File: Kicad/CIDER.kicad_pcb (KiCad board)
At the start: 2 copper layers, 0 parts

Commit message: PCB: Start routing PCB
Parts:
- added C1: 0.1u, Capacitor_SMD:C_0603_1608Metric, F.Cu at (84.9, 113.6)
- added C10: 0.1u, Capacitor_SMD:C_0603_1608Metric, F.Cu at (53.5, 110.0)
- added C11: 0.1u, Capacitor_SMD:C_0603_1608Metric, F.Cu at (76.8, 146.8)
- added C12: 0.1u, Capacitor_SMD:C_0603_1608Metric, F.Cu at (230.0, 102.8)
- added C13: 0.1u, Capacitor_SMD:C_0603_1608Metric, F.Cu at (222.0, 105.3)
- added C14: 0.1u, Capacitor_SMD:C_0603_1608Metric, F.Cu at (218.0, 102.8)
- added C15: 10u, Capacitor_SMD:C_0805_2012Metric_Pad1.18x1.45mm_HandSolder, F.Cu at (222.7, 152.0)
- added C16: 10u, Capacitor_SMD:C_0805_2012Metric_Pad1.18x1.45mm_HandSolder, F.Cu at (199.3, 183.9)
- added C17: 0.1u, Capacitor_SMD:C_0603_1608Metric, F.Cu at (207.7, 175.6)
- added C18: 0.1u, Capacitor_SMD:C_0603_1608Metric, F.Cu at (213.5, 164.9)
- added C19: 0.1u, Capacitor_SMD:C_0603_1608Metric, F.Cu at (222.3, 154.8)
- added C2: 10u, Capacitor_SMD:C_0805_2012Metric_Pad1.18x1.45mm_HandSolder, F.Cu at (86.4, 108.2)
- added C20: 0.1u, Capacitor_SMD:C_0603_1608Metric, F.Cu at (227.1, 151.8)
- added C21: 0.1u, Capacitor_SMD:C_0603_1608Metric, F.Cu at (217.5, 159.8)
- added C22: 0.1u, Capacitor_SMD:C_0603_1608Metric, F.Cu at (198.9, 186.6)
- added C23: 0.1u, Capacitor_SMD:C_0603_1608Metric, F.Cu at (213.5, 162.4)
- added C24: 0.1u, Capacitor_SMD:C_0603_1608Metric, F.Cu at (213.5, 159.8)
- added C25: 0.1u, Capacitor_SMD:C_0603_1608Metric, F.Cu at (226.3, 154.8)
- added C26: 0.1u, Capacitor_SMD:C_0603_1608Metric, F.Cu at (147.0, 165.3)
- added C27: 0.1u, Capacitor_SMD:C_0603_1608Metric, F.Cu at (131.0, 174.9)
- added C3: 0.1u, Capacitor_SMD:C_0603_1608Metric, F.Cu at (91.7, 133.6)
- added C4: 0.1u, Capacitor_SMD:C_0603_1608Metric, F.Cu at (53.5, 107.5)
- added C5: 10u, Capacitor_Tantalum_SMD:CP_EIA-3216-18_Kemet-A, F.Cu at (202.4, 95.1)
- added C6: 0.1u, Capacitor_SMD:C_0603_1608Metric, F.Cu at (87.7, 136.1)
- added C7: 0.1u, Capacitor_SMD:C_0603_1608Metric, F.Cu at (87.7, 133.6)
- added C8: 0.1u, Capacitor_SMD:C_0603_1608Metric, F.Cu at (84.9, 111.1)
- added C9: 10u, Capacitor_Tantalum_SMD:CP_EIA-3216-18_Kemet-A, F.Cu at (81.1, 108.3)
- added CN1: CDTV-DIAG, KEL-8800-080-170SF:KEL-8800-080-170S, B.Cu at (147.3, 99.1)
- added F1: Polyfuse 500mA Hold, Fuse:Fuse_1206_3216Metric, F.Cu at (245.0, 95.1)
- added J1: Conn_01x06_Male, Connector_PinHeader_2.54mm:PinHeader_1x06_P2.54mm_Vertical, F.Cu at (177.9, 106.5)
- added J2: LED, Connector_PinHeader_2.54mm:PinHeader_1x02_P2.54mm_Vertical, F.Cu at (212.2, 141.9)
- added J3: Conn_02x22_Odd_Even, Connector_PinHeader_2.00mm:PinHeader_2x22_P2.00mm_Vertical, F.Cu at (109.7, 148.0)
- added JP1: disable_ide, Connector_PinHeader_2.54mm:PinHeader_1x02_P2.54mm_Vertical, F.Cu at (77.1, 134.6)
- added JP2: configure_ram, Connector_PinHeader_2.54mm:PinHeader_1x02_P2.54mm_Vertical, F.Cu at (53.8, 98.8)
- added JP3: configure_ram, Connector_PinHeader_2.54mm:PinHeader_1x02_P2.54mm_Vertical, F.Cu at (80.6, 113.2)
- added R1: 33, Resistor_SMD:R_0603_1608Metric, F.Cu at (82.9, 139.0)
- added R10: 10K, Resistor_SMD:R_0603_1608Metric, F.Cu at (89.0, 151.4)
- added R11: 10K, Resistor_SMD:R_0603_1608Metric, F.Cu at (153.2, 151.8)
- added R2: 10k, Resistor_SMD:R_0603_1608Metric, F.Cu at (87.7, 138.6)
- added R3: 10k, Resistor_SMD:R_0603_1608Metric, F.Cu at (79.6, 119.3)
- added R4: 10k, Resistor_SMD:R_0603_1608Metric, F.Cu at (53.5, 105.0)
- added R5: 10K, Resistor_SMD:R_0603_1608Metric, F.Cu at (234.0, 102.8)
- added R6: 220, Resistor_SMD:R_0603_1608Metric, F.Cu at (238.0, 102.8)
- added R7: 10K, Resistor_SMD:R_0603_1608Metric, F.Cu at (242.0, 102.8)
- added R8: 10K, Resistor_SMD:R_0603_1608Metric, F.Cu at (226.0, 102.8)
- added R9: 10K, Resistor_SMD:R_0603_1608Metric, F.Cu at (89.2, 149.2)
- added U1: AZ1117-3.3, Package_TO_SOT_SMD:SOT-89-3, F.Cu at (77.8, 142.5)
- added U10: SST39SF010, Package_SO:TSOP-I-32_11.8x8mm_P0.5mm, F.Cu at (131.5, 125.8)
- added U2: XC95144XL-TQ100, Package_QFP:TQFP-100_14x14mm_P0.5mm, F.Cu at (164.5, 120.4)
- added U3: 74HCT245, Package_SO:TSSOP-20_4.4x6.5mm_P0.65mm, F.Cu at (116.3, 134.7)
- added U4: 74HCT245, Package_SO:TSSOP-20_4.4x6.5mm_P0.65mm, F.Cu at (116.3, 143.7)
- added U5: 74HCT245, Package_SO:TSSOP-20_4.4x6.5mm_P0.65mm, F.Cu at (116.3, 124.7)
- added U6: 74LVC245, Package_SO:TSSOP-20_4.4x6.5mm_P0.65mm, F.Cu at (144.6, 138.4)
- added U7: 74LVC245, Package_SO:TSSOP-20_4.4x6.5mm_P0.65mm, F.Cu at (144.6, 145.4)
- added U8: MT48LC4M16A2P, Package_SO:TSOP-II-54_22.2x10.16mm_P0.8mm, F.Cu at (164.5, 141.9)
- added U9: 29F160, Package_SO:TSOP-I-48_18.4x12mm_P0.5mm, F.Cu at (131.5, 112.6)
- added X1: 50MHz, Oscillator:Oscillator_SMD_Abracon_ASE-4Pin_3.2x2.5mm_HandSoldering, F.Cu at (82.5, 135.0)
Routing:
- net /Amiga+CPLD/D13: track 0.00 -> 123.7 mm, vias 0 -> 4
- net /Amiga+CPLD/D15: track 0.00 -> 123.6 mm, vias 0 -> 4
- net /Amiga+CPLD/D14: track 0.00 -> 120.0 mm, vias 0 -> 4
- net /Amiga+CPLD/D12: track 0.00 -> 119.2 mm, vias 0 -> 4
- net /Amiga+CPLD/A9: track 0.00 -> 115.6 mm, vias 0 -> 4
- net /Amiga+CPLD/D7: track 0.00 -> 112.2 mm, vias 0 -> 5
- net /Amiga+CPLD/D6: track 0.00 -> 110.9 mm, vias 0 -> 3
- net /Amiga+CPLD/A10: track 0.00 -> 108.7 mm, vias 0 -> 2
- net /Amiga+CPLD/A12: track 0.00 -> 107.5 mm, vias 0 -> 2
- net /Amiga+CPLD/D10: track 0.00 -> 106.3 mm, vias 0 -> 4
- net /Amiga+CPLD/A6: track 0.00 -> 106.3 mm, vias 0 -> 1
- net /Amiga+CPLD/D8: track 0.00 -> 105.5 mm, vias 0 -> 4
- net /Amiga+CPLD/D4: track 0.00 -> 105.1 mm, vias 0 -> 3
- net /Amiga+CPLD/D0: track 0.00 -> 104.8 mm, vias 0 -> 2
- net /Amiga+CPLD/A7: track 0.00 -> 104.6 mm, vias 0 -> 1
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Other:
- board outline added: 74.9 x 57.1 mm

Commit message: PCB: Keep on routing...
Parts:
- moved C12 112.4 mm to (119.0, 120.5), turned to 180 degrees
- moved C13 106.3 mm to (118.7, 130.4), turned to 180 degrees
- moved C14 105.8 mm to (118.7, 139.4), turned to 180 degrees
- moved C17 76.7 mm to (139.1, 141.3), turned to 180 degrees
- moved C18 76.3 mm to (139.1, 148.4), turned to 180 degrees
- moved X1 69.6 mm to (150.3, 119.1)
- moved C26 53.4 mm to (143.8, 112.0)
- moved C27 51.0 mm to (140.2, 124.8), turned to 90 degrees
- moved J1 0.96 mm to (178.4, 105.7)
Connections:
- net /Amiga+CPLD/~{FLASH_BSY} renamed Net-(R11-Pad1)
- net /Amiga+CPLD/~{IDE_IRQ} renamed /IDE/~{IDE_IRQ}
- J3 pad 38: /Amiga+CPLD/~{IDE_CS1} -> /Amiga+CPLD/~{IDE_CS2}
- U2 pad 1: unconnected-(U2-Pad1) -> /Amiga+CPLD/~{IDE_ROMCS}
- U2 pad 2: unconnected-(U2-Pad2) -> /Amiga+CPLD/~{IDE_CS1}
- U2 pad 27: unconnected-(U2-Pad27) -> /Amiga+CPLD/MEMCLK
- U2 pad 28: unconnected-(U2-Pad28) -> /Amiga+CPLD/CKE
- U2 pad 29: unconnected-(U2-Pad29) -> /Amiga+CPLD/~{RAS}
- U2 pad 3: unconnected-(U2-Pad3) -> /Amiga+CPLD/~{IDE_CS2}
- U2 pad 30: unconnected-(U2-Pad30) -> /Amiga+CPLD/~{RAMCS}
- U2 pad 32: unconnected-(U2-Pad32) -> /Amiga+CPLD/BA0
- U2 pad 33: unconnected-(U2-Pad33) -> /Amiga+CPLD/MA11
- U2 pad 34: unconnected-(U2-Pad34) -> /Amiga+CPLD/BA1
- U2 pad 35: /Amiga+CPLD/BA1 -> /Amiga+CPLD/MA9
- U2 pad 36: /Amiga+CPLD/MA9 -> /Amiga+CPLD/MA10
- U2 pad 37: /Amiga+CPLD/MA10 -> /Amiga+CPLD/MA7
- U2 pad 39: /Amiga+CPLD/MA7 -> /Amiga+CPLD/MA0
- U2 pad 4: unconnected-(U2-Pad4) -> /Amiga+CPLD/IORDY
- U2 pad 40: /Amiga+CPLD/MA0 -> /Amiga+CPLD/MA6
- U2 pad 41: /Amiga+CPLD/MA6 -> /Amiga+CPLD/MA1
- U2 pad 42: /Amiga+CPLD/MA1 -> /Amiga+CPLD/MA5
- U2 pad 43: /Amiga+CPLD/MA5 -> /Amiga+CPLD/MA2
- U2 pad 46: /Amiga+CPLD/MA2 -> /Amiga+CPLD/MA4
- U2 pad 49: /Amiga+CPLD/MA4 -> /Amiga+CPLD/MA3
- U2 pad 6: unconnected-(U2-Pad6) -> /Amiga+CPLD/~{I_BUFOE}
- U2 pad 96: unconnected-(U2-Pad96) -> /Amiga+CPLD/~{IORD}
- U2 pad 97: unconnected-(U2-Pad97) -> /Amiga+CPLD/~{FLASH_CE}
- U2 pad 99: unconnected-(U2-Pad99) -> /Amiga+CPLD/~{IOWR}
- U9 pad 16: /Amiga+CPLD/FLASH_A18 -> /Amiga+CPLD/A19
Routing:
- net /Amiga+CPLD/~{IOWR}: track 0.00 -> 115.7 mm, vias 0 -> 4
- net /Amiga+CPLD/~{IDE_CS2}: track 0.00 -> 73.9 mm, vias 0 -> 1
- net /Amiga+CPLD/~{IDE_CS1}: track 0.00 -> 69.9 mm, vias 0 -> 1
- net /Amiga+CPLD/~{IORD}: track 0.00 -> 64.9 mm, vias 0 -> 3
- net /Amiga+CPLD/R~{W}: track 30.3 -> 91.8 mm
- net /Amiga+CPLD/IORDY: track 0.00 -> 59.6 mm, vias 0 -> 1
- net /Amiga+CPLD/~{I_BUFOE}: track 0.00 -> 54.8 mm
- net /Amiga+CPLD/A19: track 29.6 -> 74.9 mm, vias 0 -> 1
- net /Amiga+CPLD/~{RST}: track 48.4 -> 83.5 mm
- net /Amiga+CPLD/~{IDE_ROMCS}: track 0.00 -> 32.9 mm, vias 0 -> 2
- net GND: track 3.99 -> 25.8 mm, vias 2 -> 18
- net /Amiga+CPLD/~{FLASH_CE}: track 0.00 -> 16.8 mm
- net VCC: track 0.00 -> 14.0 mm, vias 0 -> 5
- net /Amiga+CPLD/~{R_BUFOE}: track 0.00 -> 9.20 mm
- net /Amiga+CPLD/A17: track 90.8 -> 85.7 mm
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- added copper zone on In1.Cu, net +3.3V
- added copper zone on In2.Cu, net GND
- added copper zone on In1.Cu, net VCC
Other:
- copper layers 2 -> 4
- board text added: "1"

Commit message: PCB: More routing...
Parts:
- removed C15, C16, C2: 10u, Capacitor_SMD:C_0805_2012Metric_Pad1.18x1.45mm_HandSolder
- removed JP2: configure_ram, Connector_PinHeader_2.54mm:PinHeader_1x02_P2.54mm_Vertical
- removed R10, R11, R5, R9: 10K, Resistor_SMD:R_0603_1608Metric
- removed R2, R3, R4: 10k, Resistor_SMD:R_0603_1608Metric
- removed R6: 220, Resistor_SMD:R_0603_1608Metric
- R7, R8: moved to B.Cu
- U8: value MT48LC4M16A2P -> MT48LC8M16A2P
- moved F1 136.6 mm to (108.7, 103.2)
- moved R7 131.3 mm to (112.1, 122.0)
- moved R8 115.2 mm to (112.1, 120.0)
- moved J2 114.7 mm to (107.3, 95.5)
- moved C10 113.2 mm to (164.5, 131.7), turned to 180 degrees
- moved C4 104.3 mm to (157.6, 113.0), turned to 135 degrees
- moved JP1 101.9 mm to (178.4, 123.6)
- moved JP3 99.4 mm to (178.4, 131.0)
- moved C7 89.2 mm to (175.9, 120.4), turned to -45 degrees
- moved C6 88.6 mm to (173.7, 115.2), turned to 45 degrees
- moved C8 88.4 mm to (171.7, 127.6), turned to -45 degrees
- moved C11 80.2 mm to (153.7, 124.0), turned to 180 degrees
- moved R1 76.0 mm to (158.5, 131.3)
- moved U1 70.0 mm to (145.3, 123.9), turned to -90 degrees
- moved C1 69.8 mm to (153.6, 126.0), turned to 180 degrees
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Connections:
- JP1 pad 1: unconnected-(JP1-Pad1) -> /Amiga+CPLD/~{IDE_OFF}
- JP3 pad 1: unconnected-(JP3-Pad1) -> /Amiga+CPLD/RAM_J1
- U2 pad 1: /Amiga+CPLD/~{IDE_ROMCS} -> /Amiga+CPLD/~{IOWR}
- U2 pad 18: unconnected-(U2-Pad18) -> /Amiga+CPLD/~{R_BUFOE}
- U2 pad 19: unconnected-(U2-Pad19) -> /Amiga+CPLD/DQML
- U2 pad 20: unconnected-(U2-Pad20) -> /Amiga+CPLD/RAM_~{W}
- U2 pad 22: unconnected-(U2-Pad22) -> /Amiga+CPLD/DQMH
- U2 pad 23: unconnected-(U2-Pad23) -> /Amiga+CPLD/MEMCLK
- U2 pad 24: unconnected-(U2-Pad24) -> /Amiga+CPLD/~{CAS}
- U2 pad 25: unconnected-(U2-Pad25) -> /Amiga+CPLD/~{RAS}
- U2 pad 27: /Amiga+CPLD/MEMCLK -> /Amiga+CPLD/CKE
- U2 pad 28: /Amiga+CPLD/CKE -> /Amiga+CPLD/~{RAMCS}
- U2 pad 29: /Amiga+CPLD/~{RAS} -> /Amiga+CPLD/BA0
- U2 pad 30: /Amiga+CPLD/~{RAMCS} -> /Amiga+CPLD/MA11
- U2 pad 32: /Amiga+CPLD/BA0 -> /Amiga+CPLD/BA1
- U2 pad 33: /Amiga+CPLD/MA11 -> /Amiga+CPLD/MA9
- U2 pad 34: /Amiga+CPLD/BA1 -> /Amiga+CPLD/MA10
- U2 pad 35: /Amiga+CPLD/MA9 -> /Amiga+CPLD/MA8
- U2 pad 36: /Amiga+CPLD/MA10 -> /Amiga+CPLD/MA0
- U2 pad 39: /Amiga+CPLD/MA0 -> /Amiga+CPLD/MA1
- U2 pad 41: /Amiga+CPLD/MA1 -> /Amiga+CPLD/MA2
- U2 pad 43: /Amiga+CPLD/MA2 -> /Amiga+CPLD/MA3
- U2 pad 49: /Amiga+CPLD/MA3 -> /Amiga+CPLD/RAM_J1
- U2 pad 50: /Amiga+CPLD/MA8 -> /Amiga+CPLD/~{IDE_OFF}
- U2 pad 99: /Amiga+CPLD/~{IOWR} -> /Amiga+CPLD/~{IDE_ROMCS}
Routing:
- net +3.3V: track 3.75 -> 54.3 mm, vias 2 -> 17
- net GND: track 25.8 -> 68.7 mm, vias 18 -> 48
- net /Amiga+CPLD/R~{W}: track 91.8 -> 132.8 mm, vias 0 -> 2
- net /IDE/B_~{RESET}: track 29.9 -> 0.00 mm
- net /Amiga+CPLD/~{R_BUFOE}: track 9.20 -> 36.2 mm
- net /Amiga+CPLD/MA3: track 0.00 -> 25.1 mm
- net /Amiga+CPLD/MA2: track 0.00 -> 24.6 mm
- net /Amiga+CPLD/MA1: track 0.00 -> 24.3 mm
- net /Amiga+CPLD/DQML: track 0.00 -> 22.4 mm
- net /Amiga+CPLD/RAM_~{W}: track 0.00 -> 22.3 mm
- net /Amiga+CPLD/MA0: track 0.00 -> 22.1 mm
- net /Amiga+CPLD/~{RAS}: track 0.00 -> 21.6 mm
- net /Amiga+CPLD/MA10: track 0.00 -> 21.3 mm
- net /Amiga+CPLD/~{CAS}: track 0.00 -> 20.7 mm
- net /Amiga+CPLD/BA1: track 0.00 -> 20.6 mm
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
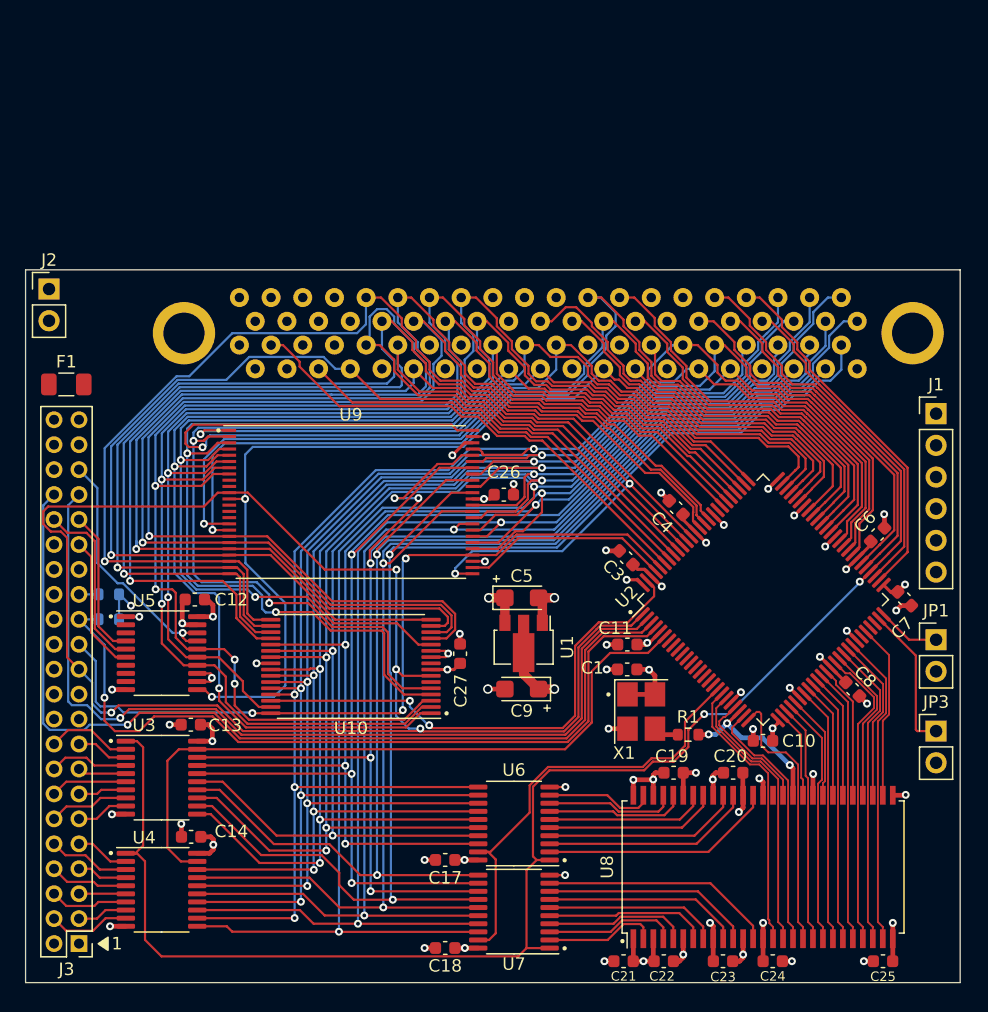
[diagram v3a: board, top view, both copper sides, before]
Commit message: PCB: More work...
* Add DIP Switches for Ram/Rom/IDE config
* Route bank select signals for Flash rom
* Flip IDE to bottom of the board
* Add some bulk capacitors
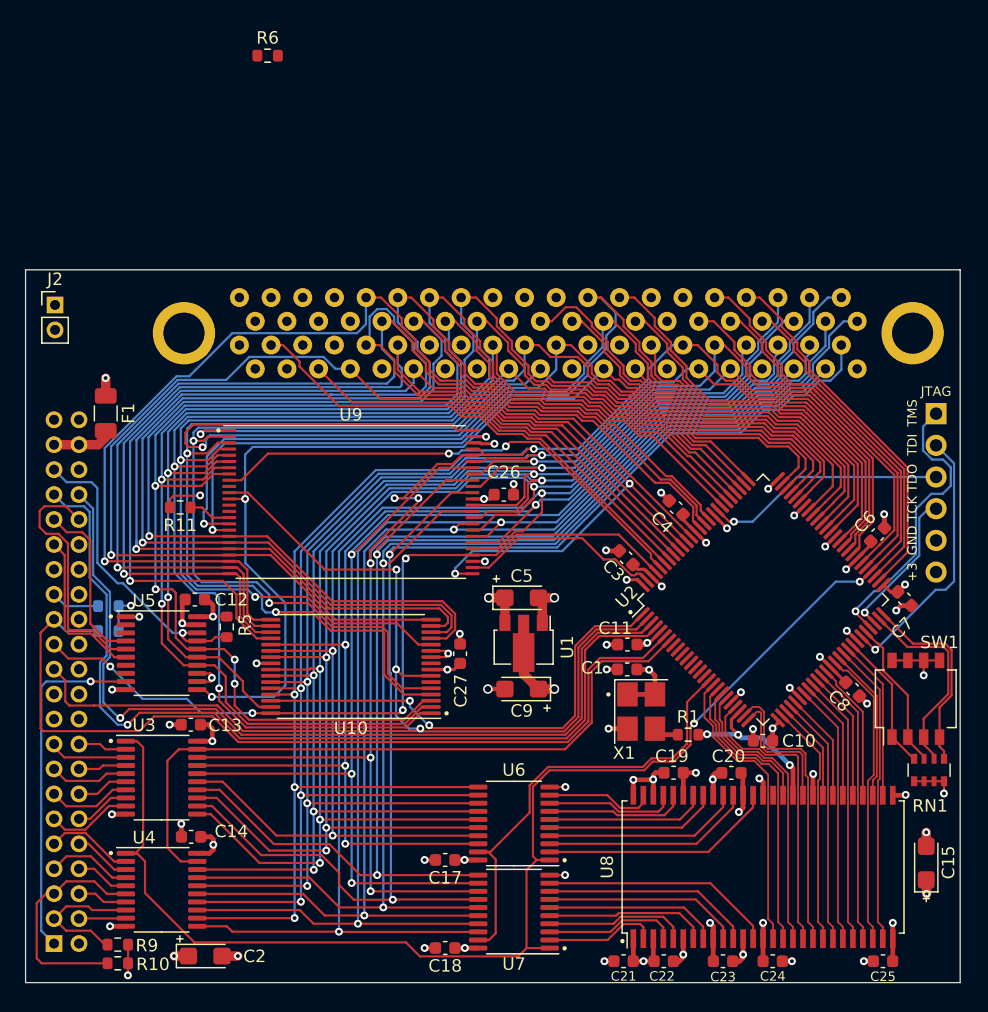
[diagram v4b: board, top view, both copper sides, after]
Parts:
- removed JP1: disable_ide, Connector_PinHeader_2.54mm:PinHeader_1x02_P2.54mm_Vertical
- removed JP3: configure_ram, Connector_PinHeader_2.54mm:PinHeader_1x02_P2.54mm_Vertical
- added C15: 10u, Capacitor_Tantalum_SMD:CP_EIA-3216-18_Kemet-A, F.Cu at (177.6, 141.5)
- added C2: 10u, Capacitor_Tantalum_SMD:CP_EIA-3216-18_Kemet-A, F.Cu at (119.8, 149.0)
- added R10: 10K, Resistor_SMD:R_0603_1608Metric, F.Cu at (112.8, 149.6)
- added R11: 10K, Resistor_SMD:R_0603_1608Metric, F.Cu at (117.8, 113.0)
- added R5: 10K, Resistor_SMD:R_0603_1608Metric, F.Cu at (121.5, 122.6)
- added R6: 220, Resistor_SMD:R_0603_1608Metric, F.Cu at (124.8, 76.8)
- added R9: 10K, Resistor_SMD:R_0603_1608Metric, F.Cu at (112.8, 148.1)
- added RN1: R_Pack04, Resistor_SMD:R_Array_Convex_4x0603, F.Cu at (177.9, 134.1)
- added SW1: SW_DIP_x04, Button_Switch_SMD:SW_DIP_SPSTx04_Slide_Omron_A6H-4101_W6.15mm_P1.27mm, F.Cu at (176.8, 128.4)
- J1: value Conn_01x06_Male -> JTAG
- J2: footprint Connector_PinHeader_2.54mm:PinHeader_1x02_P2.54mm_Vertical -> Connector_PinHeader_2.00mm:PinHeader_1x02_P2.00mm_Vertical
- J3: moved to B.Cu
- moved F1 3.92 mm to (111.8, 105.5), turned to -90 degrees
- moved J3 2.00 mm to (107.7, 148.0), turned to 0 degrees
- moved J2 1.36 mm to (107.8, 96.8)
- moved R7 0.95 mm to (112.0, 122.9)
- moved R8 0.95 mm to (112.0, 120.9)
- moved C20 0.14 mm to (162.0, 134.3)
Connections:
- U2 pad 1: /Amiga+CPLD/~{IOWR} -> /Amiga+CPLD/~{IDE_ROMCS}
- U2 pad 16: unconnected-(U2-Pad16) -> /Amiga+CPLD/~{R_BUFOE}
- U2 pad 17: unconnected-(U2-Pad17) -> /Amiga+CPLD/DQML
- U2 pad 18: /Amiga+CPLD/~{R_BUFOE} -> /Amiga+CPLD/RAM_~{W}
- U2 pad 19: /Amiga+CPLD/DQML -> /Amiga+CPLD/DQMH
- U2 pad 2: /Amiga+CPLD/~{IDE_CS1} -> /Amiga+CPLD/~{IOWR}
- U2 pad 20: /Amiga+CPLD/RAM_~{W} -> /Amiga+CPLD/~{CAS}
- U2 pad 22: /Amiga+CPLD/DQMH -> /Amiga+CPLD/~{RAS}
- U2 pad 24: /Amiga+CPLD/~{CAS} -> /Amiga+CPLD/~{RAMCS}
- U2 pad 25: /Amiga+CPLD/~{RAS} -> /Amiga+CPLD/CKE
- U2 pad 27: /Amiga+CPLD/CKE -> /Amiga+CPLD/BA0
- U2 pad 28: /Amiga+CPLD/~{RAMCS} -> /Amiga+CPLD/MA11
- U2 pad 29: /Amiga+CPLD/BA0 -> /Amiga+CPLD/BA1
- U2 pad 30: /Amiga+CPLD/MA11 -> /Amiga+CPLD/MA9
- U2 pad 32: /Amiga+CPLD/BA1 -> /Amiga+CPLD/MA10
- U2 pad 33: /Amiga+CPLD/MA9 -> /Amiga+CPLD/MA8
- U2 pad 34: /Amiga+CPLD/MA10 -> /Amiga+CPLD/MA0
- U2 pad 35: /Amiga+CPLD/MA8 -> /Amiga+CPLD/MA7
- U2 pad 36: /Amiga+CPLD/MA0 -> /Amiga+CPLD/MA1
- U2 pad 37: /Amiga+CPLD/MA7 -> /Amiga+CPLD/MA6
- U2 pad 39: /Amiga+CPLD/MA1 -> /Amiga+CPLD/MA2
- U2 pad 4: /Amiga+CPLD/IORDY -> /Amiga+CPLD/~{IDE_CS1}
- U2 pad 40: /Amiga+CPLD/MA6 -> /Amiga+CPLD/MA5
- U2 pad 41: /Amiga+CPLD/MA2 -> /Amiga+CPLD/MA3
- U2 pad 42: /Amiga+CPLD/MA5 -> /Amiga+CPLD/MA4
- U2 pad 43: /Amiga+CPLD/MA3 -> /Amiga+CPLD/~{RAM_EN}
- U2 pad 46: /Amiga+CPLD/MA4 -> /Amiga+CPLD/~{RANGER_EN}
- U2 pad 49: /Amiga+CPLD/RAM_J1 -> /Amiga+CPLD/~{IDE_EN}
- U2 pad 50: /Amiga+CPLD/~{IDE_OFF} -> /Amiga+CPLD/~{FLASH_EN}
- U2 pad 6: /Amiga+CPLD/~{I_BUFOE} -> /Amiga+CPLD/IORDY
- U2 pad 7: unconnected-(U2-Pad7) -> /Amiga+CPLD/~{I_BUFOE}
- U2 pad 96: /Amiga+CPLD/~{IORD} -> /Amiga+CPLD/FLASH_A19
- U2 pad 97: /Amiga+CPLD/~{FLASH_CE} -> /Amiga+CPLD/~{IORD}
- U2 pad 99: /Amiga+CPLD/~{IDE_ROMCS} -> /Amiga+CPLD/~{FLASH_CE}
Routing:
- net /Amiga+CPLD/FLASH_A19: track 0.00 -> 40.2 mm, vias 0 -> 2
- net /Amiga+CPLD/~{IOWR}: track 119.0 -> 90.9 mm, vias 4 -> 3
- net /IDE/B_~{RESET}: track 0.00 -> 28.0 mm, vias 0 -> 1
- net /Amiga+CPLD/TMS: track 0.00 -> 23.4 mm, vias 0 -> 1
- net /Amiga+CPLD/TDI: track 0.00 -> 22.2 mm, vias 0 -> 1
- net /Amiga+CPLD/TDO: track 0.00 -> 19.4 mm, vias 0 -> 1
- net /Amiga+CPLD/~{IDE_EN}: track 0.00 -> 16.4 mm
- net /Amiga+CPLD/~{FLASH_EN}: track 0.00 -> 15.9 mm
- net /IDE/B_D14: track 3.74 -> 18.6 mm
- net /Amiga+CPLD/TCK: track 0.00 -> 12.2 mm, vias 0 -> 1
- net /Amiga+CPLD/~{RANGER_EN}: track 0.00 -> 12.1 mm
- net /Amiga+CPLD/RAM_J1: track 11.8 -> 0.00 mm
- net /Amiga+CPLD/~{RAM_EN}: track 0.00 -> 11.2 mm
- net VCC: track 21.5 -> 30.6 mm, vias 8 -> 12
- net /IDE/B_D15: track 4.04 -> 11.4 mm
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- added copper zone on In2.Cu, net +3.3V
- added copper zone on In1.Cu, net GND
- added copper zone on In2.Cu, net VCC
- removed copper zone on In1.Cu, net +3.3V
- removed copper zone on In2.Cu, net GND
- removed copper zone on In1.Cu, net VCC
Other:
- board text added: "+3"
- board text added: "GND"
- board text added: "TCK"
- board text added: "TDI"
- board text added: "TDO"
- board text added: "TMS"
